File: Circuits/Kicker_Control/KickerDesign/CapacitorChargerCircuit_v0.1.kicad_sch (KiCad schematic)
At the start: 14 parts, among them Q2 NMOS, T1 DA2034-ALD

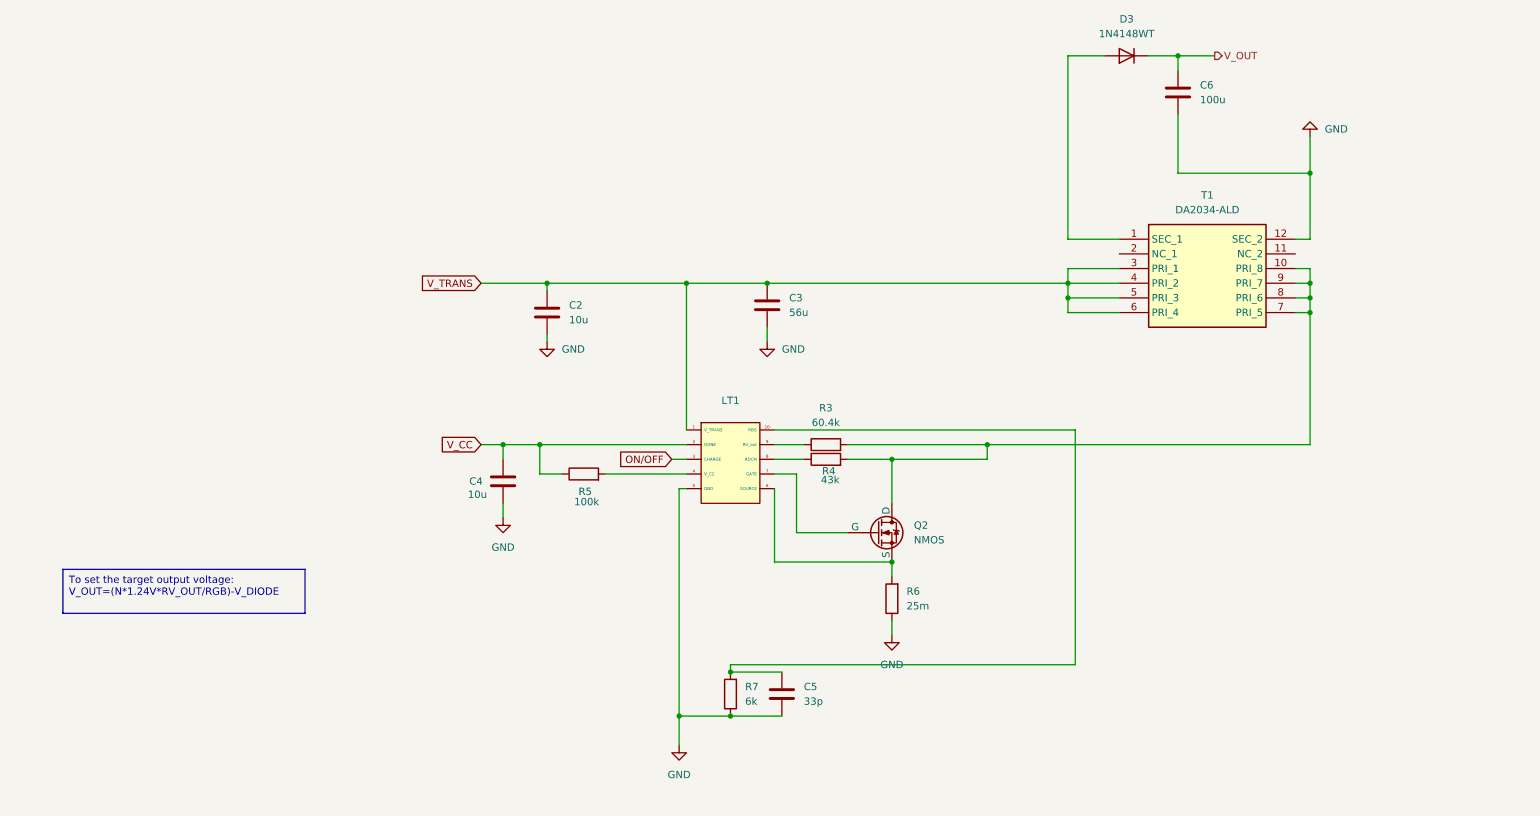
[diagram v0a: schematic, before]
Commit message: Added a discharge circuit for saftey reasons to the capacitor charger
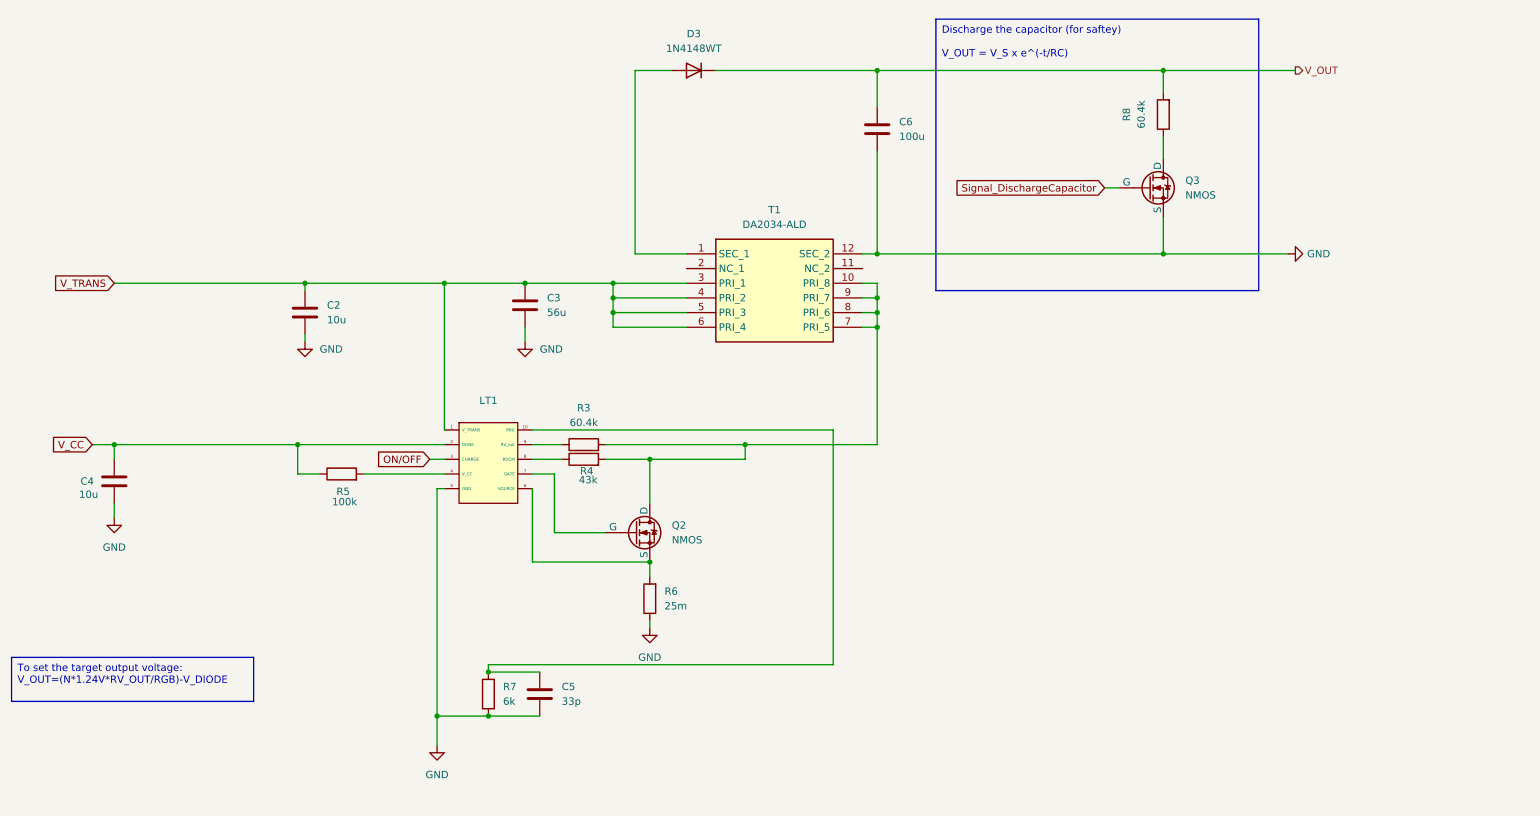
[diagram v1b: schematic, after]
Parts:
- added Q3: NMOS, symbol Simulation_SPICE:NMOS
- added R8: 60.4k, symbol Device:R
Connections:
- net GND: now also Q3.3 (S)
- net V_OUT: now also R8.2
- new net: Q3.1 (D), R8.1
- new net Signal_DischargeCapacitor: Q3.2 (G)
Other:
- moved on the sheet: C2, C3, C4, C5, C6, D3, LT1, Q2, R3, R4, R5, R6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

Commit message: Added a circuit and made some small changes in the kicker circuit
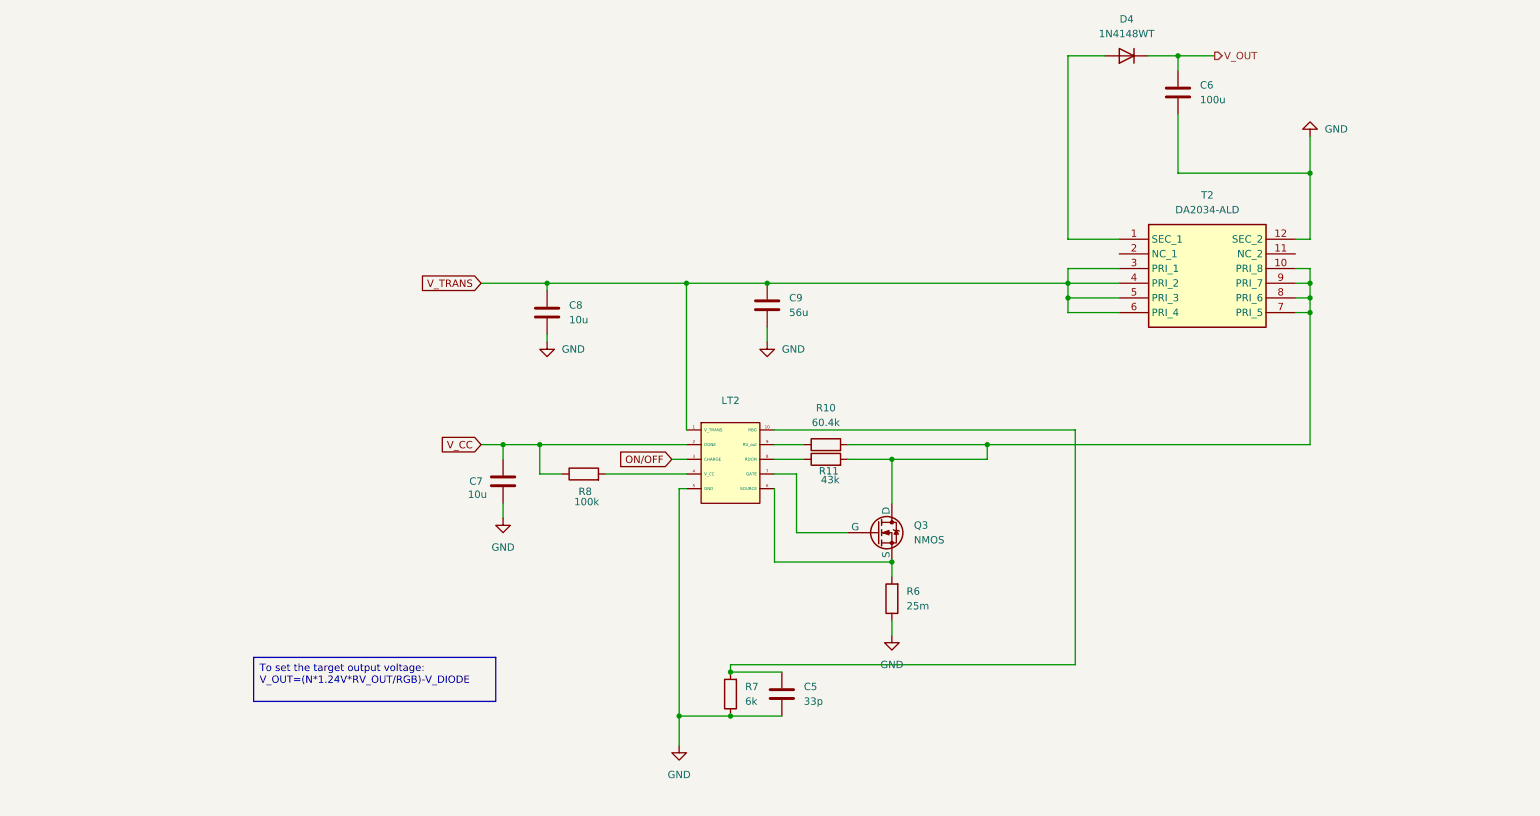
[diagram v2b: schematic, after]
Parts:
- removed Q3: NMOS, symbol Simulation_SPICE:NMOS
- removed R8: 60.4k, symbol Device:R
- renumbered C4 to C7, C2 to C8, C3 to C9, D3 to D4, LT1 to LT2, Q2 to Q3, R3 to R10, R4 to R11, R5 to R8, T1 to T2
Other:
- moved on the sheet: C5, C6, C7, C8, C9, D4, LT2, Q3, R10, R11, R6, R7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

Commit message: Made changes in the circuit
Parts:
- added Q2: NMOS, symbol Simulation_SPICE:NMOS
- added R3: 100k, symbol Device:R
- added R4, R5: 33k, symbol Device:R
- added R9: ¨33k, symbol Device:R
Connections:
- net GND: now also Q2.3 (S)
- net V_OUT: now also R3.2, R4.2, R5.2, R9.2
- new net: Q2.1 (D), R3.1, R4.1, R5.1, R9.1
- new net Signal: Q2.2 (G)
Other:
- moved on the sheet: C5, C6, D4, R7, T2

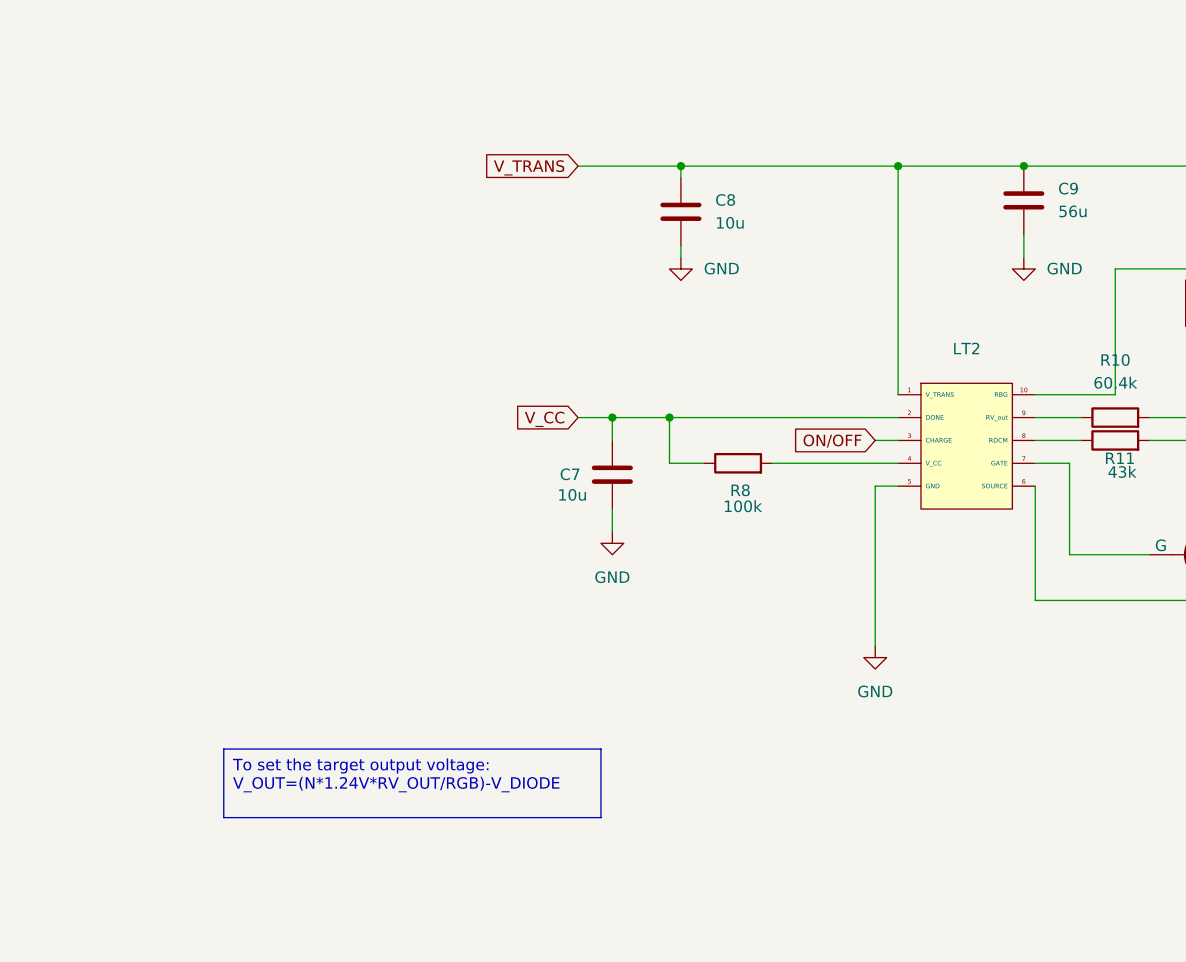
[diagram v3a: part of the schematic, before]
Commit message: Updated kicker circuit
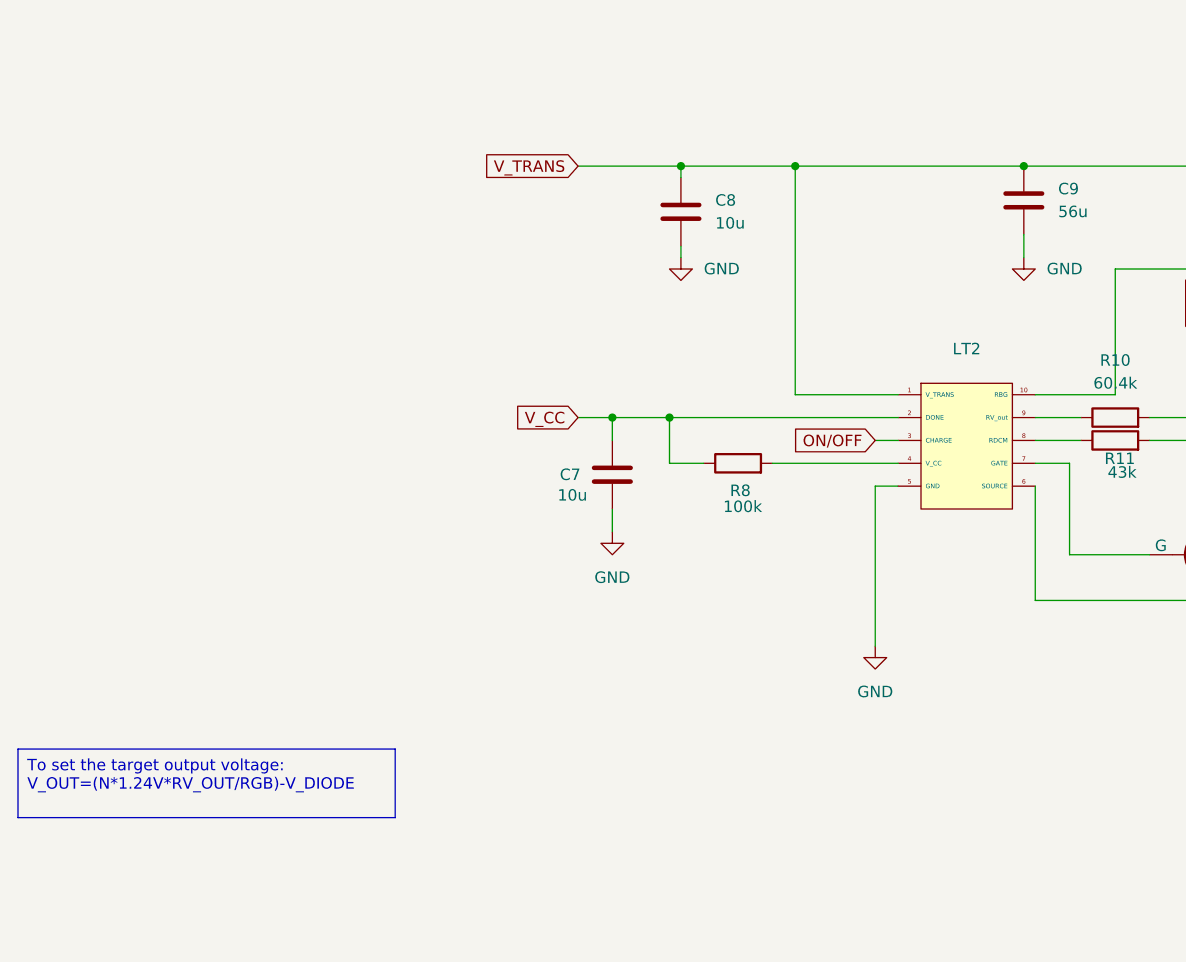
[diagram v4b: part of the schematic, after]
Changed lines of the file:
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@@
-	)
-	(junction
-		(at 137.16 62.23)
-		(diameter 0)
-		(color 0 0 0 0)
 	)
 	(junction
@@
 	)
 	(junction
+		(at 125.73 62.23)
+		(diameter 0)
+		(color 0 0 0 0)
+	)
+	(junction
 		(at 236.22 120.65)
 		(diameter 0)
@@
 	(wire
 		(pts
+			(xy 125.73 62.23) (xy 151.13 62.23)
+		)
+		(stroke
+			(width 0)
+			(type default)
+		)
+	)
+	(wire
+		(pts
 			(xy 243.84 22.86) (xy 243.84 107.95)
 		)
@@
 	(wire
 		(pts
-			(xy 137.16 62.23) (xy 151.13 62.23)
-		)
-		(stroke
-			(width 0)
-			(type default)
-		)
-	)
-	(wire
-		(pts
 			(xy 165.1 90.17) (xy 189.23 90.17)
 		)
@@
 	(wire
 		(pts
+			(xy 125.73 87.63) (xy 137.16 87.63)
+		)
+		(stroke
+			(width 0)
+			(type default)
+		)
+	)
+	(wire
+		(pts
 			(xy 101.6 90.17) (xy 105.41 90.17)
 		)
@@
 	(wire
 		(pts
-			(xy 137.16 87.63) (xy 137.16 62.23)
+			(xy 125.73 87.63) (xy 125.73 62.23)
 		)
 		(stroke
@@
 	(wire
 		(pts
-			(xy 113.03 62.23) (xy 137.16 62.23)
+			(xy 113.03 62.23) (xy 125.73 62.23)
 		)
 		(stroke
@@
 	(text_box "To set the target output voltage: \nV_OUT=(N*1.24V*RV_OUT/RGB)-V_DIODE"
 		(exclude_from_sim no)
-		(at 62.23 127 0)
+		(at 39.37 127 0)
 		(size 41.91 7.62)
 		(stroke
